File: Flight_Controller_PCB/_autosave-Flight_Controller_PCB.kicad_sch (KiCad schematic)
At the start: 7 parts, among them J1 USB_C_Receptacle, SW1 SW_Push, U2 MPU-6050, U3 MS5611-01BA, U4 INA226, U5 NEO-M8N, U6 CP2102N-Axx-xQFN24

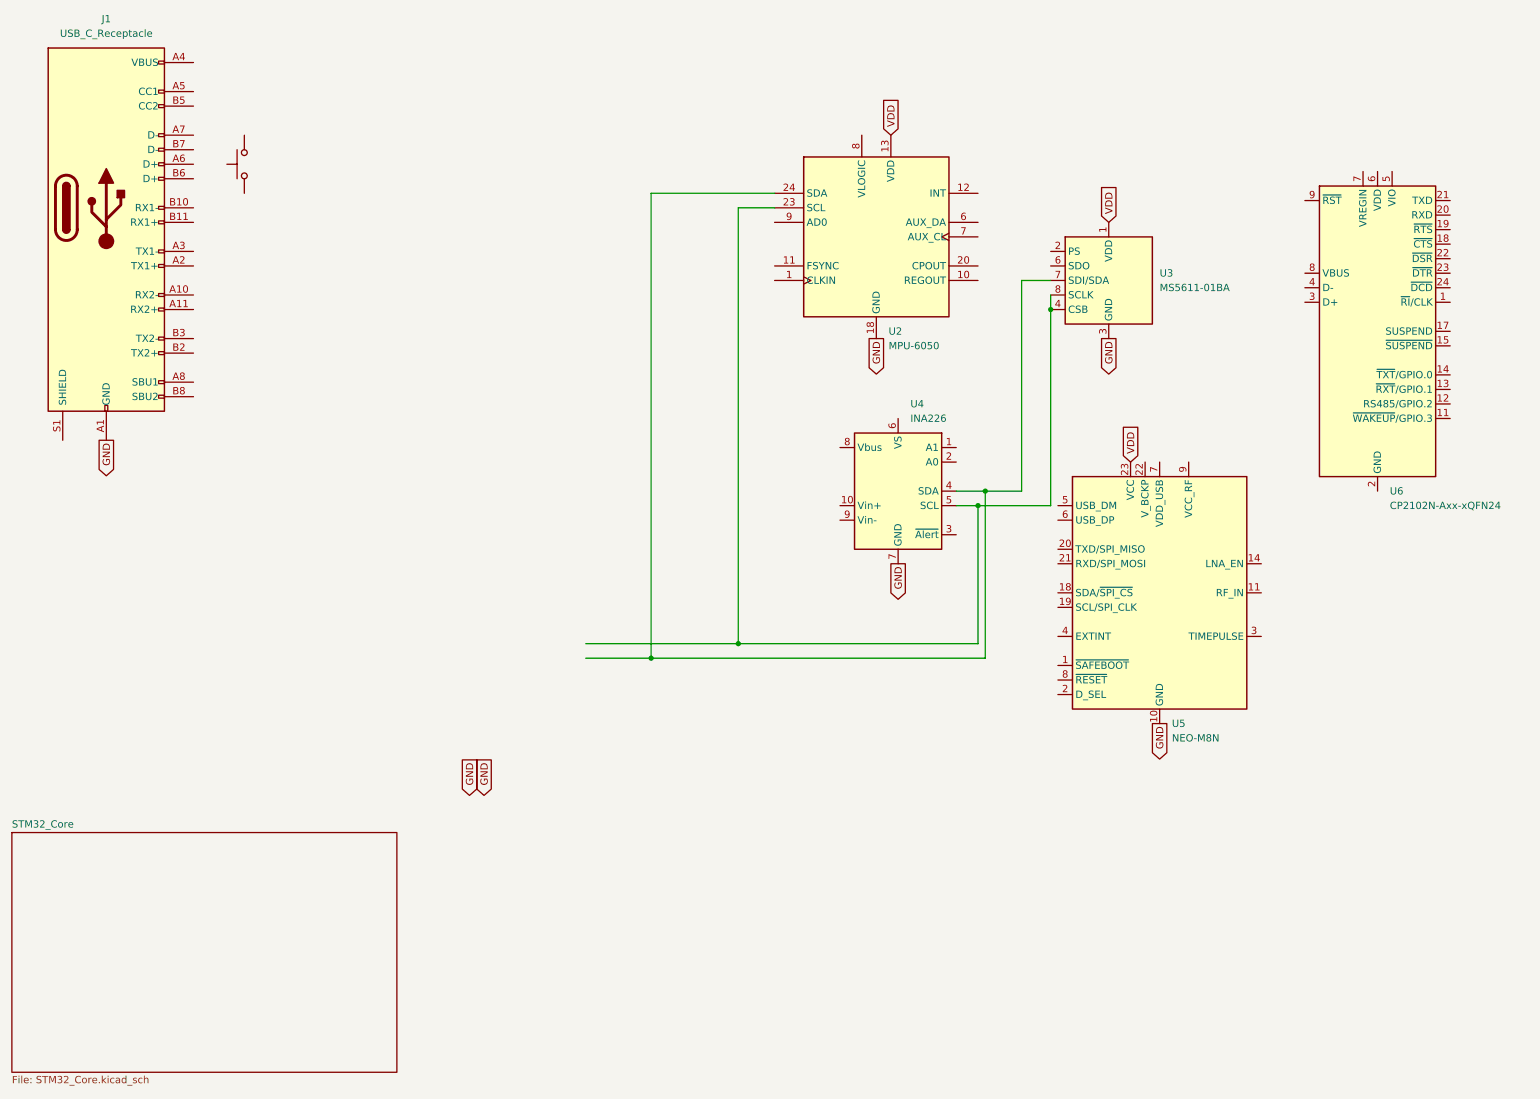
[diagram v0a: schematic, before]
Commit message: Refactor telemetry system and improve UART communication
- Added telemetry functionality with structured packet format for sending flight data.
- Implemented DMA for USART1 to enhance data transmission efficiency.
- Adjusted UART baud rate to 460800 for higher data throughput.
- Introduced TIM5 for accurate timing and delta time calculations.
- Updated motor control functions to use float instead of double for consistency.
- Modified SPI settings for improved communication with nRF24L01+ module.
- Enhanced error handling and added callbacks for UART transmission completion.
- Cleaned up commented-out code and improved overall code readability.
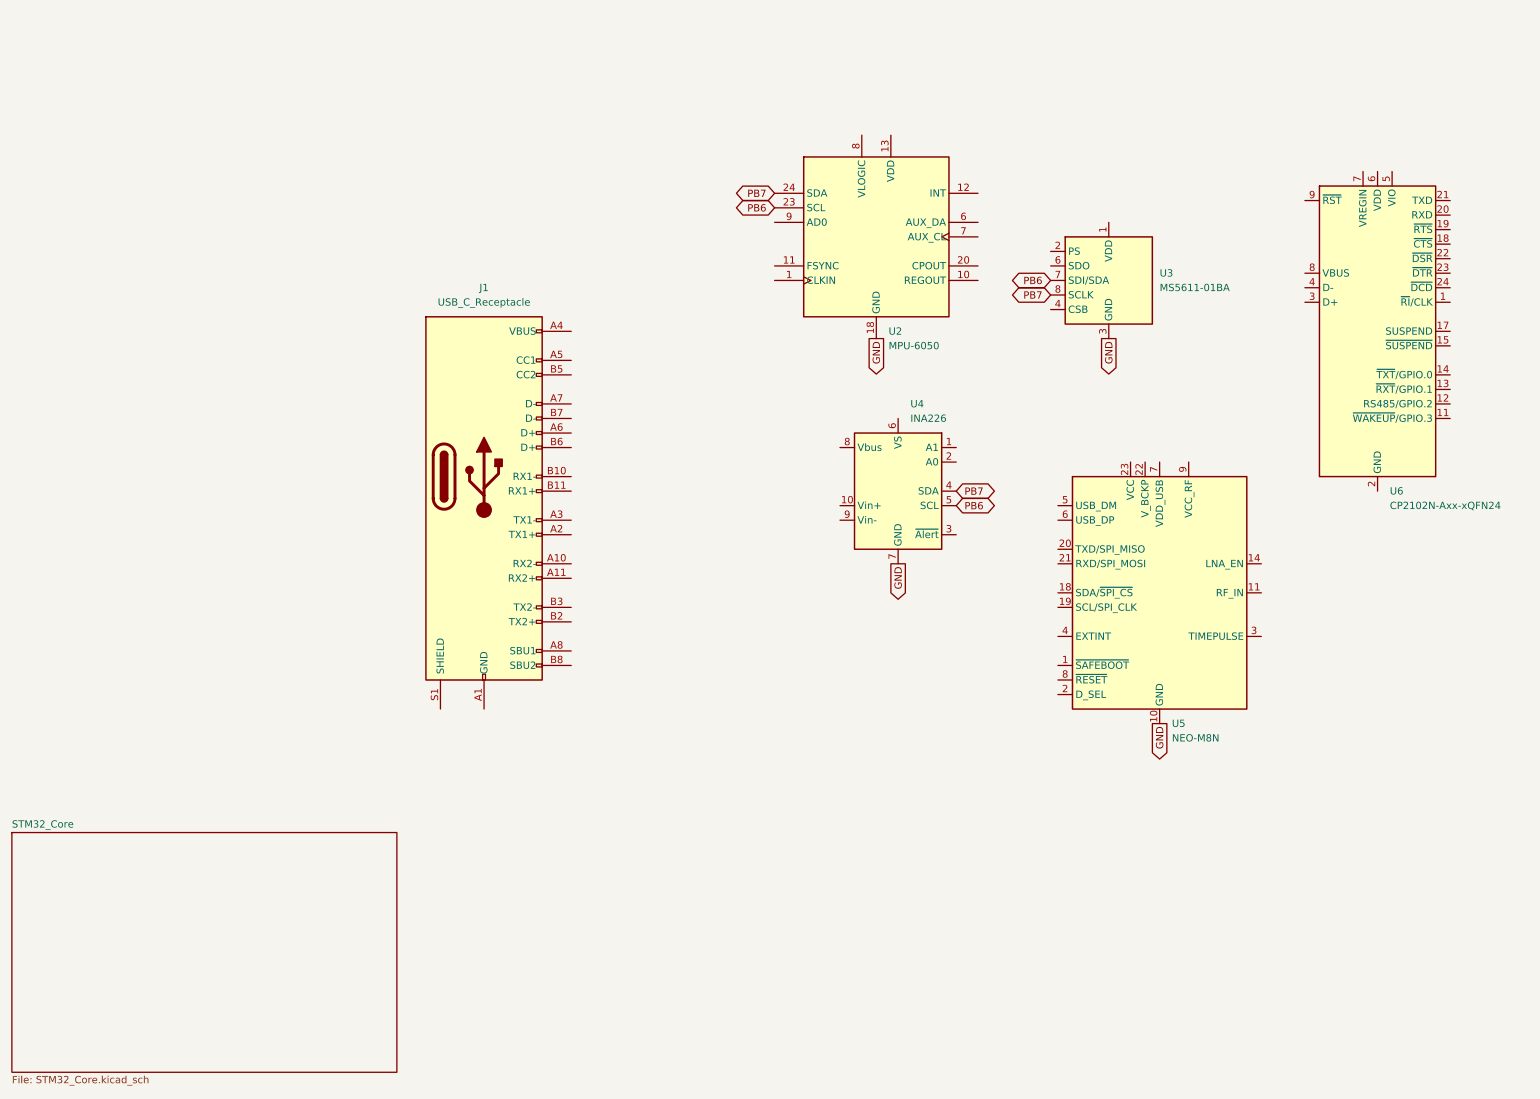
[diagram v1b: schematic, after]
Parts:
- removed SW1: SW_Push, symbol Switch:SW_Push
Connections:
- net GND: no longer J1.A1 (GND), J1.A12 (GND), J1.B1 (GND), J1.B12 (GND)
- net PB7: now reaches U2.24 (SDA), U4.4 (SDA)
- net PB7: now also U3.8 (SCLK); no longer U3.7 (SDI/SDA)
- removed net VDD: U2.13 (VDD), U3.1 (VDD), U5.23 (VCC)
- new net: J1.A1 (GND), J1.A12 (GND), J1.B1 (GND), J1.B12 (GND)
- new net: U3.4 (CSB), U3.5 (CSB)
- new net PB6: U2.23 (SCL), U3.7 (SDI/SDA), U4.5 (SCL)
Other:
- moved on the sheet: J1
